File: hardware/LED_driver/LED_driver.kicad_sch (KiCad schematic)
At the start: 6 parts, among them Q2 IRF4905

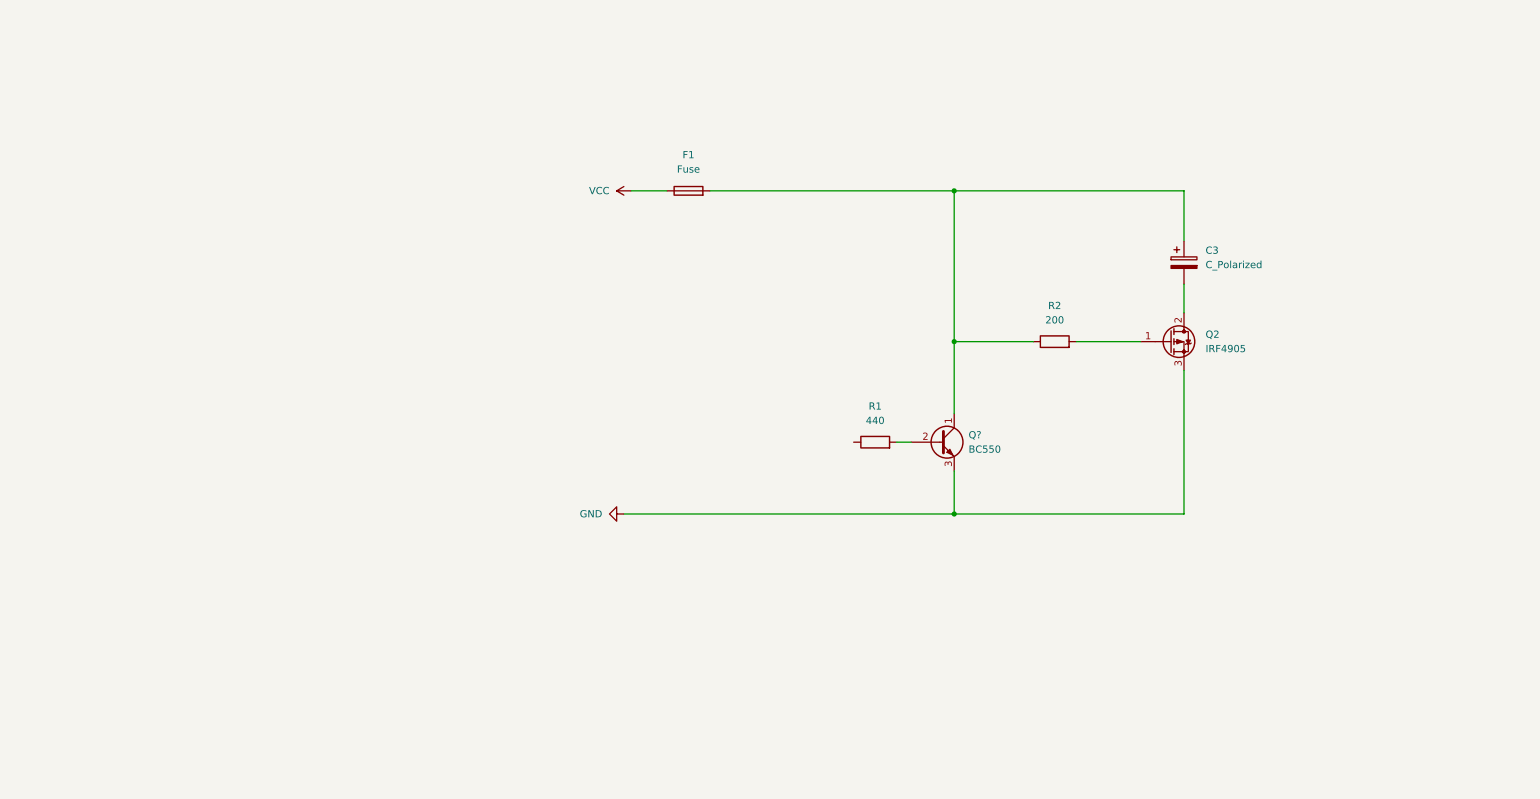
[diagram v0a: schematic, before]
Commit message: programmmin for esp is still not included, not tested
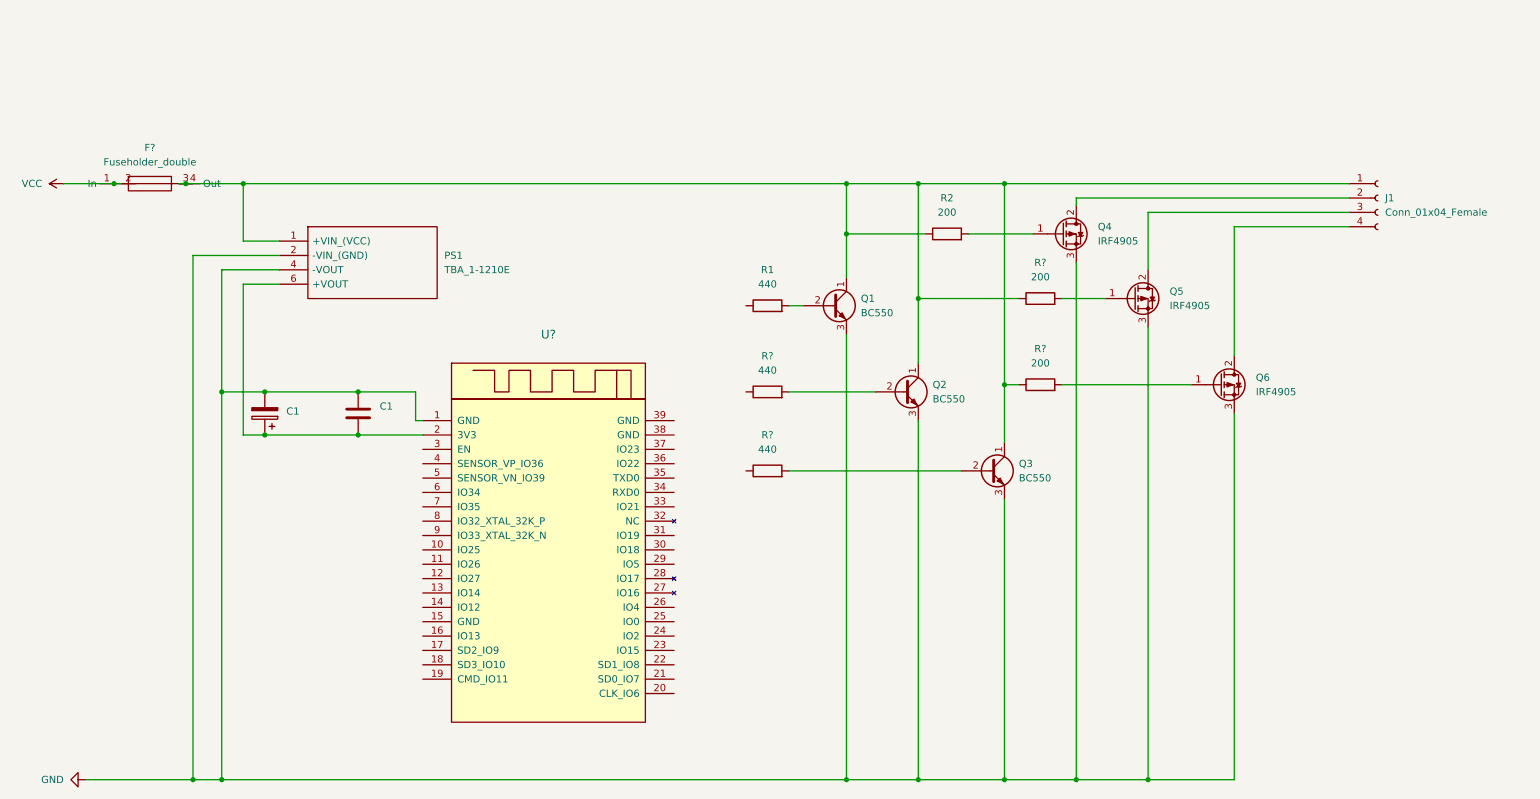
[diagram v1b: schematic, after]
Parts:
- removed C3: C_Polarized, symbol Device:C_Polarized
- removed F1: Fuse, symbol Device:Fuse
- added C1: (no value), symbol Device:C
- added C1: (no value), symbol Device:C_Polarized
- added F?: Fuseholder_double, symbol New_Library:Fuseholder_double
- added J1: Conn_01x04_Female, symbol Connector:Conn_01x04_Female
- added PS1: TBA_1-1210E, TBA11210E, symbol SamacSys_Parts:TBA_1-1210E
- added Q2, Q3: BC550, Package_TO_SOT_THT:TO-92_Inline, symbol Transistor_BJT:BC550
- added Q5, Q6: IRF4905, Package_TO_SOT_THT:TO-220-3_Vertical, symbol Transistor_FET:IRF4905
- added R? (x2): 200, symbol Device:R
- added R? (x2): 440, symbol Device:R
- added U?: (no value), symbol ESP-32_E:ESP32-WROVER
- gave numbers to parts that had none: 1
- renumbered Q2 to Q4
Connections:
- net GND: now also C1.1, C1.2, PS1.2 (-VIN_(GND)), PS1.4 (-VOUT), Q2.3 (E), Q3.3 (E), Q5.3 (S), Q6.3 (S), U?.1 (GND)
- net VCC: now also F?.1 (In), F?.2
- net at Q1.1 (C), R2.1: now also F?.3, F?.4 (Out), J1.1 (Pin_1), PS1.1 (+VIN_(VCC)), Q2.1 (C), Q3.1 (C), R?.1, R?.1
- net at Q4.2 (D): now also J1.2 (Pin_2)
- new net: Q3.2 (B), R?.2
- new net: C1.1, C1.2, PS1.6 (+VOUT), U?.2 (3V3)
- new net: Q6.1 (G), R?.2
- new net: Q5.1 (G), R?.2
- new net: J1.3 (Pin_3), Q5.2 (D)
- new net: Q2.2 (B), R?.2
- new net: J1.4 (Pin_4), Q6.2 (D)
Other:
- moved on the sheet: Q1, Q4, R1, R2

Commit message: finished PCB
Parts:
- removed PS1: TBA_1-1210E, TBA11210E, symbol SamacSys_Parts:TBA_1-1210E
- removed U?: (no value), symbol ESP-32_E:ESP32-WROVER
- added C3, C4: 100nF, Capacitor_SMD:C_0603_1608Metric, symbol Device:C
- added C5: 22µF, Capacitor_SMD:CP_Elec_5x5.3, symbol Device:C_Polarized
- added C6: 22pF, Capacitor_SMD:C_0603_1608Metric, symbol Device:C
- added J1: (no value), symbol Connector:Conn_01x02_Female
- added J2: UART, Connector_PinHeader_2.54mm:PinHeader_2x02_P2.54mm_Vertical, symbol Connector:Conn_01x04_Female
- added L1: (no value), symbol Device:L
- added R1: 100k, Resistor_SMD:R_0603_1608Metric, symbol Device:R
- added R2: 22,1k, Resistor_SMD:R_0603_1608Metric, symbol Device:R
- added R3: 10k, Resistor_SMD:R_0603_1608Metric, symbol Device:R
- added R4: 499, Resistor_SMD:R_0603_1608Metric, symbol Device:R
- added S1: RST, Library:SW-SMD-2.9x3.9x1,7, symbol New_Library:Switch
- added S2: BOOT, Library:SW-SMD-2.9x3.9x1,7, symbol New_Library:Switch
- added T1: SY8120, Package_TO_SOT_SMD:SOT-23-6, symbol New_Library:SY8120
- added U1: (no value), symbol RF_Module:ESP32-WROOM-32D
- C1: value (none) -> 22µF; footprint (none) -> Capacitor_SMD:CP_Elec_5x5.3
- C2: renamed from C1; value (none) -> 100nF; footprint (none) -> Capacitor_SMD:C_0603_1608Metric
- F1: renamed from F?; footprint (none) -> Library:Fuseholder 5x20
- J3: renamed from J1; value Conn_01x04_Female -> LED; footprint (none) -> Connector_PinHeader_2.54mm:PinHeader_1x04_P2.54mm_Vertical
- Q1, Q3: value BC550 -> (none); footprint Package_TO_SOT_THT:TO-92_Inline -> (none)
- Q2: footprint Package_TO_SOT_THT:TO-92_Inline -> Package_TO_SOT_THT:TO-92
- R10, R7, R8, R9: renamed from R?; footprint (none) -> Resistor_SMD:R_0603_1608Metric
- R5: renamed from R1; footprint (none) -> Resistor_SMD:R_0603_1608Metric
- R6: renamed from R2; footprint (none) -> Resistor_SMD:R_0603_1608Metric
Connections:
- net GND: now also C3.2, C5.2, J1.2 (Pin_2), J2.2 (Pin_2), R2.2, S1.2 (Out), S2.2 (Out), T1.2 (GND), U1.1 (GND), U1.15 (GND), U1.38 (GND), U1.39 (GND)
- net VCC: now also J1.1 (Pin_1)
- net at F1.3, F1.4 (Out), J3.1 (Pin_1)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: now also C5.1, R3.1, T1.4 (EN), T1.5 (IN)
- net at C1.1, C2.2: now also C6.1, J2.1 (Pin_1), L1.2, R1.1, U1.2 (VDD)
- net at R5.1: now also U1.28 (IO17)
- net at R9.1: now also U1.31 (IO19)
- net at R7.1: now also U1.30 (IO18)
- new net: R4.1, U1.35 (TXD0/IO1)
- new net: J2.3 (Pin_3), R4.2
- new net: C3.1, R3.2, S1.1 (In), U1.3 (EN)
- new net: C6.2, R1.2, R2.1, T1.3 (FB)
- new net: C4.2, L1.1, T1.6 (LX)
- new net: J2.4 (Pin_4), U1.34 (RXD0/IO3)
- new net: C4.1, T1.1 (BS)
- new net: S2.1 (In), U1.25 (IO0)
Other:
- moved on the sheet: C1, C2, J3, Q1, Q2, Q3, Q4, Q5, Q6, R10, R5, R6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
